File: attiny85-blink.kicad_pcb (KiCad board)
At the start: 2 copper layers, 30 x 17.8 mm, 4 parts, among them J1 AVR-ISP-6, U1 ATtiny85-20PU

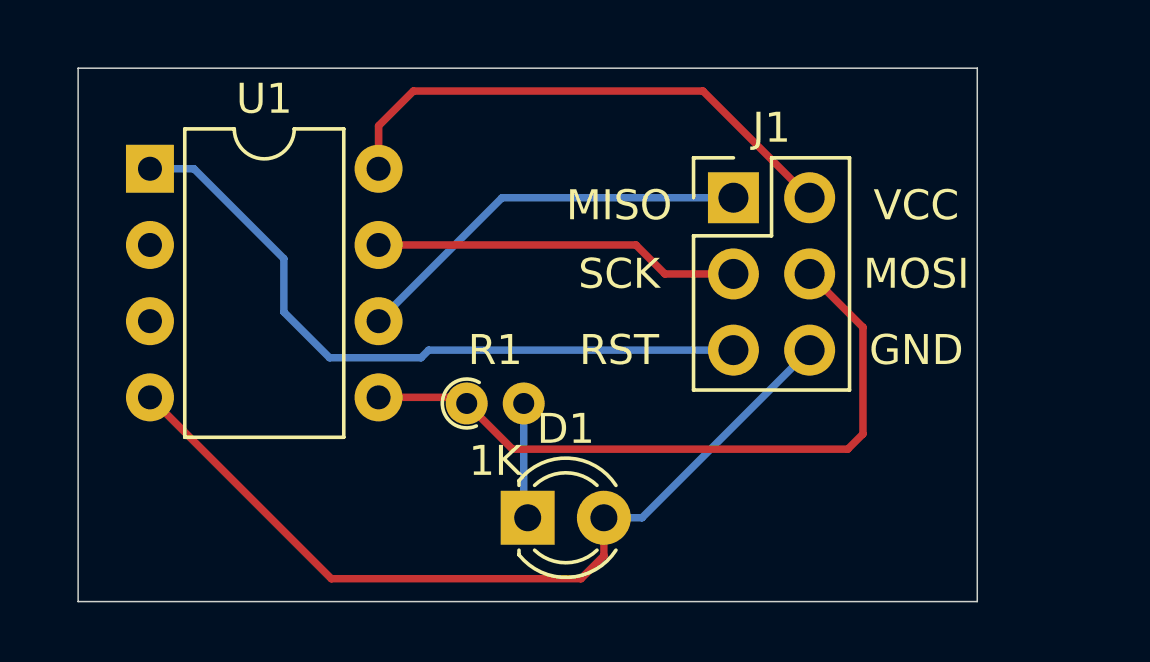
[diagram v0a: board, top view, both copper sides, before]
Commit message: Added VCC and GND to schematic, moved around traces and made copper pours on PCB.
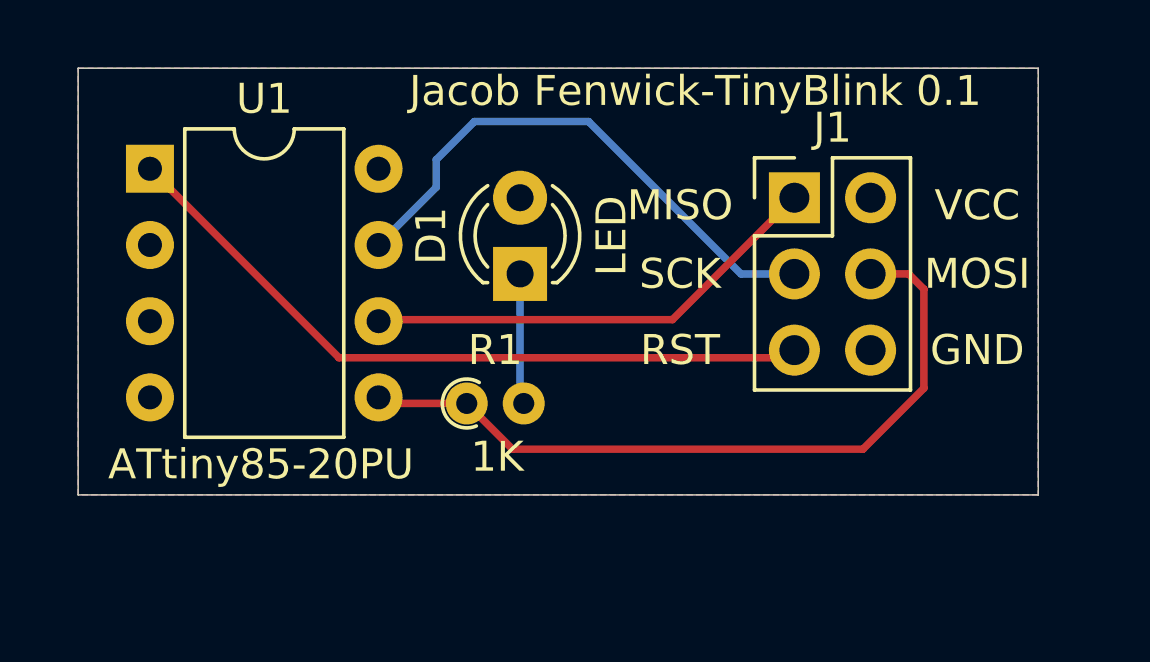
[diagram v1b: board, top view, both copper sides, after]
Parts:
- moved D1 8.13 mm to (95.5, 148.3), turned to 90 degrees
- moved J1 2.03 mm to (104.6, 145.8)
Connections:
- net Net-(D1-Pad2) renamed GND
- net Net-(J1-Pad2) renamed VCC
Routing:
- net GND: track 28.4 -> 0.00 mm
- net VCC: track 17.8 -> 0.00 mm
- net Net-(J1-Pad3): track 12.2 -> 18.2 mm
- net Net-(J1-Pad4): track 23.4 -> 25.6 mm
- net Net-(J1-Pad1): track 13.5 -> 15.6 mm
- net Net-(J1-Pad5): track 23.9 -> 25.2 mm
- net Net-(D1-Pad1): track 3.86 -> 4.54 mm
- added copper zone on B.Cu, net GND
- added copper zone on F.Cu, net VCC
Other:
- board size 30 x 17.8 mm -> 32 x 14.2 mm
- board text added: "ATtiny85-20PU"
- board text added: "Jacob Fenwick-TinyBlink 0.1"
- board text added: "LED"
